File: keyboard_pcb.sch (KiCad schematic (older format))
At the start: 4 parts, among them J1 Conn_01x04_Female, J2 , J3 Conn_01x03_Male, U1 Teensy4.0

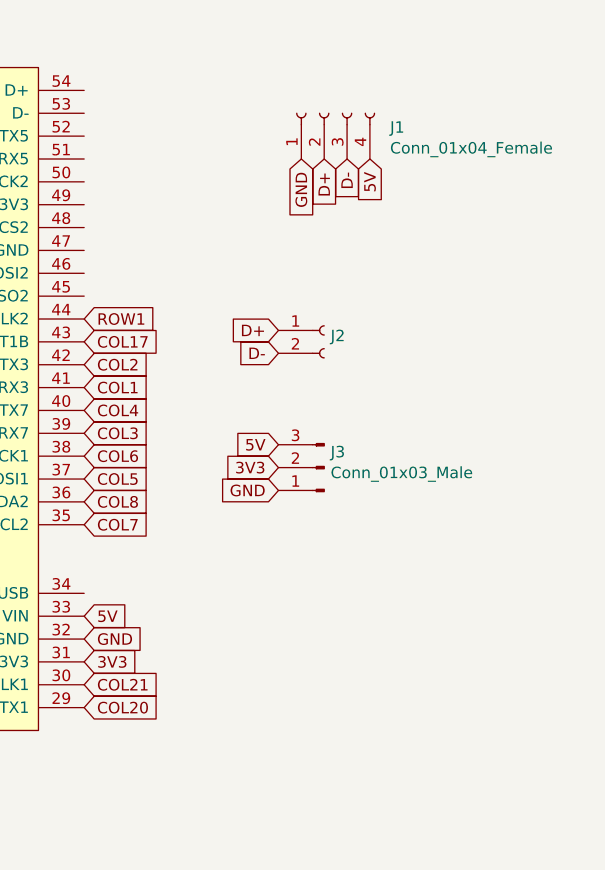
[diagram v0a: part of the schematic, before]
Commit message: Fixed missing connections and schematic changes
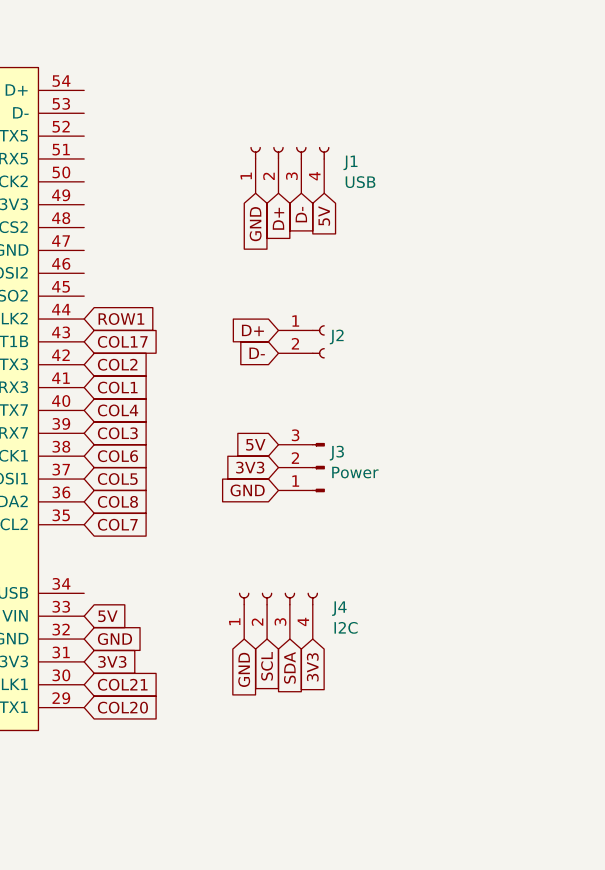
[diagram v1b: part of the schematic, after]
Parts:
- added J4: I2C, Connector_PinHeader_2.54mm:PinHeader_1x04_P2.54mm_Vertical, symbol Connector:Conn_01x04_Female
- J1: value Conn_01x04_Female -> USB
- J3: value Conn_01x03_Male -> Power
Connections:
- net 3V3: now also J4.4 (Pin_4)
- net GND: now also J4.1 (Pin_1)
- net SCL: now also J4.2 (Pin_2)
- net SDA: now also J4.3 (Pin_3)
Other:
- moved on the sheet: J1
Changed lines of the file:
@@
 L Connector:Conn_01x04_Female J1
 U 1 1 61DA0AF6
-P 7750 2100
-F 0 "J1" V 7688 1812 50  0000 R CNN
-F 1 "Conn_01x04_Female" V 7597 1812 50  0000 R CNN
-F 2 "Connector_PinHeader_2.54mm:PinHeader_1x04_P2.54mm_Vertical" H 7750 2100 50  0001 C CNN
-F 3 "~" H 7750 2100 50  0001 C CNN
-	1    7750 2100
+P 7550 2250
+F 0 "J1" V 7488 1962 50  0000 R CNN
+F 1 "USB" V 7397 1962 50  0000 R CNN
+F 2 "Connector_PinHeader_2.54mm:PinHeader_1x04_P2.54mm_Vertical" H 7550 2250 50  0001 C CNN
+F 3 "~" H 7550 2250 50  0001 C CNN
+	1    7550 2250
 	0    -1   -1   0
 $EndComp
-Text GLabel 7650 2300 3    50   Input ~ 0
+Text GLabel 7450 2450 3    50   Input ~ 0
 GND
-Text GLabel 7750 2300 3    50   Input ~ 0
+Text GLabel 7550 2450 3    50   Input ~ 0
 D+
-Text GLabel 7850 2300 3    50   Input ~ 0
+Text GLabel 7650 2450 3    50   Input ~ 0
 D-
-Text GLabel 7950 2300 3    50   Input ~ 0
+Text GLabel 7750 2450 3    50   Input ~ 0
 5V
 $Comp
@@
 P 7750 3650
 F 0 "J3" H 7722 3582 50  0000 R CNN
-F 1 "Conn_01x03_Male" H 7722 3673 50  0000 R CNN
+F 1 "Power" H 7722 3673 50  0000 R CNN
 F 2 "Connector_PinHeader_2.54mm:PinHeader_1x03_P2.54mm_Vertical" H 7750 3650 50  0001 C CNN
 F 3 "~" H 7750 3650 50  0001 C CNN
@@
 Text GLabel 6700 4700 2    50   Input ~ 0
 COL20
+$Comp
+L Connector:Conn_01x04_Female J4
+U 1 1 61E417AE
+P 7500 4200
+F 0 "J4" V 7438 3912 50  0000 R CNN
+F 1 "I2C" V 7347 3912 50  0000 R CNN
+F 2 "Connector_PinHeader_2.54mm:PinHeader_1x04_P2.54mm_Vertical" H 7500 4200 50  0001 C CNN
+F 3 "~" H 7500 4200 50  0001 C CNN
+	1    7500 4200
+	0    -1   -1   0
+$EndComp
+Text GLabel 7400 4400 3    50   Input ~ 0
+GND
+Text GLabel 7500 4400 3    50   Input ~ 0
+SCL
+Text GLabel 7600 4400 3    50   Input ~ 0
+SDA
+Text GLabel 7700 4400 3    50   Input ~ 0
+3V3
 $EndSCHEMATC
